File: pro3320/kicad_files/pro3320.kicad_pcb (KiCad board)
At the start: 2 copper layers, 68.3 x 99.1 mm, 82 parts, among them J1 RES_CV, J2 IN, J3 FREQ_CV, J4 EUROPOWER, J5 OUT, J6 OUT2, SW1 LPHP2, SW2 LPHP1, SW3 LPHP3, SW4 LPHP4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

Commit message: pro3320: Fix wrong direction of pots
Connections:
- RV1 pad 1: Net-(R1-Pad2) -> GND
- RV1 pad 3: GND -> Net-(R1-Pad2)
- RV2 pad 1: Net-(J3-Pad2) -> GND
- RV2 pad 3: GND -> Net-(J3-Pad2)
- RV3 pad 1: Net-(J1-Pad2) -> GND
- RV3 pad 3: GND -> Net-(J1-Pad2)
- RV4 pad 1: Net-(C1-Pad2) -> GND
- RV4 pad 3: GND -> Net-(C1-Pad2)
- RV5 pad 1: Net-(R8-Pad1) -> GND
- RV5 pad 3: GND -> Net-(R8-Pad1)
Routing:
- net Net-(R1-Pad2): track 12.5 -> 20.0 mm
- net Net-(J1-Pad2): track 130.5 -> 135.0 mm
- net Net-(J3-Pad2): track 96.7 -> 100.7 mm
- net Net-(R8-Pad1): track 5.17 -> 8.17 mm
- net Net-(C1-Pad2): track 5.04 -> 7.38 mm
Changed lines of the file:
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@@
     (thickness 1.6)
     (drawings 10)
-    (tracks 479)
+    (tracks 484)
     (zones 0)
     (modules 82)
@@
     )
     (pad 3 thru_hole circle (at 0 5) (size 1.8 1.8) (drill 1) (layers *.Cu *.Mask)
-      (net 8 GND))
+      (net 16 "Net-(R1-Pad2)"))
     (pad 2 thru_hole circle (at 0 2.5) (size 1.8 1.8) (drill 1) (layers *.Cu *.Mask)
       (net 19 "Net-(R4-Pad1)"))
     (pad 1 thru_hole circle (at 0 0) (size 1.8 1.8) (drill 1) (layers *.Cu *.Mask)
-      (net 16 "Net-(R1-Pad2)"))
+      (net 8 GND))
     (model ${KISYS3DMOD}/Potentiometer_THT.3dshapes/Potentiometer_Alps_RK097_Single_Horizontal.wrl
       (at (xyz 0 0 0))
@@
     (fp_line (start -2.05 7.25) (end -2.05 -2.25) (layer B.Fab) (width 0.1))
     (pad 1 thru_hole circle (at 0 0) (size 1.8 1.8) (drill 1) (layers *.Cu *.Mask)
-      (net 56 "Net-(J3-Pad2)"))
+      (net 8 GND))
     (pad 2 thru_hole circle (at 0 2.5) (size 1.8 1.8) (drill 1) (layers *.Cu *.Mask)
       (net 20 "Net-(R5-Pad1)"))
     (pad 3 thru_hole circle (at 0 5) (size 1.8 1.8) (drill 1) (layers *.Cu *.Mask)
-      (net 8 GND))
+      (net 56 "Net-(J3-Pad2)"))
     (model ${KISYS3DMOD}/Potentiometer_THT.3dshapes/Potentiometer_Alps_RK097_Single_Horizontal.wrl
       (at (xyz 0 0 0))
@@
     (fp_line (start -2.05 7.25) (end -2.05 -2.25) (layer B.Fab) (width 0.1))
     (pad 1 thru_hole circle (at 0 0) (size 1.8 1.8) (drill 1) (layers *.Cu *.Mask)
-      (net 55 "Net-(J1-Pad2)"))
+      (net 8 GND))
     (pad 2 thru_hole circle (at 0 2.5) (size 1.8 1.8) (drill 1) (layers *.Cu *.Mask)
       (net 27 "Net-(R12-Pad1)"))
     (pad 3 thru_hole circle (at 0 5) (size 1.8 1.8) (drill 1) (layers *.Cu *.Mask)
-      (net 8 GND))
+      (net 55 "Net-(J1-Pad2)"))
     (model ${KISYS3DMOD}/Potentiometer_THT.3dshapes/Potentiometer_Alps_RK097_Single_Horizontal.wrl
       (at (xyz 0 0 0))
@@
     )
     (pad 3 thru_hole circle (at 0 5) (size 1.8 1.8) (drill 1) (layers *.Cu *.Mask)
-      (net 8 GND))
+      (net 1 "Net-(C1-Pad2)"))
     (pad 2 thru_hole circle (at 0 2.5) (size 1.8 1.8) (drill 1) (layers *.Cu *.Mask)
       (net 49 "Net-(RV4-Pad2)"))
     (pad 1 thru_hole circle (at 0 0) (size 1.8 1.8) (drill 1) (layers *.Cu *.Mask)
-      (net 1 "Net-(C1-Pad2)"))
+      (net 8 GND))
     (model ${KISYS3DMOD}/Potentiometer_THT.3dshapes/Potentiometer_Alps_RK097_Single_Horizontal.wrl
       (at (xyz 0 0 0))
@@
     )
     (pad 3 thru_hole circle (at 0 5) (size 1.8 1.8) (drill 1) (layers *.Cu *.Mask)
-      (net 8 GND))
+      (net 22 "Net-(R8-Pad1)"))
     (pad 2 thru_hole circle (at 0 2.5) (size 1.8 1.8) (drill 1) (layers *.Cu *.Mask)
       (net 26 "Net-(R11-Pad1)"))
     (pad 1 thru_hole circle (at 0 0) (size 1.8 1.8) (drill 1) (layers *.Cu *.Mask)
-      (net 22 "Net-(R8-Pad1)"))
+      (net 8 GND))
     (model ${KISYS3DMOD}/Potentiometer_THT.3dshapes/Potentiometer_Alps_RK097_Single_Horizontal.wrl
       (at (xyz 0 0 0))
@@
   (gr_line (start 155.956 40.64) (end 155.956 139.7) (layer Edge.Cuts) (width 0.15))
   (segment (start 146.465 43.053) (end 146.018 43.5) (width 0.25) (layer F.Cu) (net 1))
-  (segment (start 150.876 43.053) (end 146.465 43.053) (width 0.25) (layer F.Cu) (net 1))
+  (segment (start 150.571 48.053) (end 150.876 48.053) (width 0.25) (layer B.Cu) (net 1))
+  (segment (start 146.018 43.5) (end 150.571 48.053) (width 0.25) (layer B.Cu) (net 1))
   (segment (start 140.02 43.5) (end 139.7 43.18) (width 0.25) (layer F.Cu) (net 2))
   (segment (start 144.018 43.5) (end 140.02 43.5) (width 0.25) (layer F.Cu) (net 2))
@@
   (segment (start 138.906 119.888) (end 137.382 118.364) (width 0.25) (layer F.Cu) (net 15))
   (segment (start 138.906 125.222) (end 138.906 119.888) (width 0.25) (layer F.Cu) (net 15))
-  (segment (start 145.325999 56.171999) (end 144.526 55.372) (width 0.25) (layer F.Cu) (net 16))
-  (segment (start 149.849001 60.695001) (end 145.325999 56.171999) (width 0.25) (layer F.Cu) (net 16))
-  (segment (start 149.849001 64.378001) (end 149.849001 60.695001) (width 0.25) (layer F.Cu) (net 16))
-  (segment (start 150.749 65.278) (end 149.849001 64.378001) (width 0.25) (layer F.Cu) (net 16))
+  (segment (start 145.325999 56.171999) (end 144.526 55.372) (width 0.25) (layer B.Cu) (net 16))
+  (segment (start 153.797 64.643) (end 145.325999 56.171999) (width 0.25) (layer B.Cu) (net 16))
+  (segment (start 153.797 67.23) (end 153.797 64.643) (width 0.25) (layer B.Cu) (net 16))
+  (segment (start 150.749 70.278) (end 153.797 67.23) (width 0.25) (layer B.Cu) (net 16))
   (segment (start 141.478 64.516) (end 144.526 61.468) (width 0.25) (layer F.Cu) (net 17))
   (segment (start 136.906 64.516) (end 141.478 64.516) (width 0.25) (layer F.Cu) (net 17))
@@
   (segment (start 150.876 97.79) (end 154.12001 94.54599) (width 0.25) (layer F.Cu) (net 18))
   (segment (start 154.12001 94.54599) (end 154.12001 75.49599) (width 0.25) (layer F.Cu) (net 18))
-  (segment (start 149.849001 66.878001) (end 149.682001 66.878001) (width 0.25) (layer F.Cu) (net 19))
-  (segment (start 150.749 67.778) (end 149.849001 66.878001) (width 0.25) (layer F.Cu) (net 19))
-  (segment (start 149.682001 66.878001) (end 148.336 65.532) (width 0.25) (layer F.Cu) (net 19))
-  (segment (start 148.336 62.23) (end 144.526 58.42) (width 0.25) (layer F.Cu) (net 19))
-  (segment (start 148.336 65.532) (end 148.336 62.23) (width 0.25) (layer F.Cu) (net 19))
+  (segment (start 149.849001 66.878001) (end 149.682001 66.878001) (width 0.25) (layer B.Cu) (net 19))
+  (segment (start 150.749 67.778) (end 149.849001 66.878001) (width 0.25) (layer B.Cu) (net 19))
+  (segment (start 149.682001 66.878001) (end 148.336 65.532) (width 0.25) (layer B.Cu) (net 19))
+  (segment (start 148.336 62.23) (end 144.526 58.42) (width 0.25) (layer B.Cu) (net 19))
+  (segment (start 148.336 65.532) (end 148.336 62.23) (width 0.25) (layer B.Cu) (net 19))
   (segment (start 149.849001 111.328001) (end 149.849001 111.241001) (width 0.25) (layer F.Cu) (net 20))
   (segment (start 150.749 112.228) (end 149.849001 111.328001) (width 0.25) (layer F.Cu) (net 20))
@@
   (segment (start 123.19 50.8) (end 127.762 50.8) (width 0.25) (layer B.Cu) (net 21))
   (segment (start 147.193 87.503) (end 146.05 86.36) (width 0.25) (layer F.Cu) (net 22))
-  (segment (start 150.749 87.503) (end 147.193 87.503) (width 0.25) (layer F.Cu) (net 22))
+  (segment (start 147.193 89.027) (end 147.193 87.503) (width 0.25) (layer F.Cu) (net 22))
+  (segment (start 150.749 92.583) (end 147.193 89.027) (width 0.25) (layer F.Cu) (net 22))
   (segment (start 130.81 54.61) (end 131.826 55.626) (width 0.25) (layer F.Cu) (net 23))
   (segment (start 130.81 50.8) (end 130.81 54.61) (width 0.25) (layer F.Cu) (net 23))
@@
   (segment (start 102.362 106.172) (end 100.33 108.204) (width 0.25) (layer B.Cu) (net 54))
   (segment (start 112.288 114.3) (end 104.16 106.172) (width 0.25) (layer B.Cu) (net 54))
-  (segment (start 155.448 41.91) (end 154.57801 41.04001) (width 0.25) (layer F.Cu) (net 55))
-  (segment (start 155.448 129.54) (end 155.448 41.91) (width 0.25) (layer F.Cu) (net 55))
-  (segment (start 154.57801 41.04001) (end 121.51999 41.04001) (width 0.25) (layer F.Cu) (net 55))
   (segment (start 121.51999 41.04001) (end 119.38 43.18) (width 0.25) (layer F.Cu) (net 55))
-  (segment (start 153.035 131.953) (end 155.448 129.54) (width 0.25) (layer F.Cu) (net 55))
-  (segment (start 150.876 131.953) (end 153.035 131.953) (width 0.25) (layer F.Cu) (net 55))
-  (segment (start 152.4 109.728) (end 150.749 109.728) (width 0.25) (layer F.Cu) (net 56))
-  (segment (start 154.94 107.188) (end 152.4 109.728) (width 0.25) (layer F.Cu) (net 56))
-  (segment (start 154.99799 42.22199) (end 154.99799 53.28201) (width 0.25) (layer F.Cu) (net 56))
-  (segment (start 154.26602 41.49002) (end 154.99799 42.22199) (width 0.25) (layer F.Cu) (net 56))
-  (segment (start 154.99799 53.28201) (end 154.94 53.34) (width 0.25) (layer F.Cu) (net 56))
-  (segment (start 131.22998 41.49002) (end 154.26602 41.49002) (width 0.25) (layer F.Cu) (net 56))
-  (segment (start 154.94 53.34) (end 154.94 107.188) (width 0.25) (layer F.Cu) (net 56))
-  (segment (start 129.54 43.18) (end 131.22998 41.49002) (width 0.25) (layer F.Cu) (net 56))
+  (segment (start 154.57801 41.04001) (end 121.51999 41.04001) (width 0.25) (layer F.Cu) (net 55))
+  (segment (start 152.654 136.447792) (end 152.654 132.334) (width 0.25) (layer F.Cu) (net 55))
+  (segment (start 155.448 129.54) (end 155.448 41.91) (width 0.25) (layer F.Cu) (net 55))
+  (segment (start 152.148792 136.953) (end 152.654 136.447792) (width 0.25) (layer F.Cu) (net 55))
+  (segment (start 155.448 41.91) (end 154.57801 41.04001) (width 0.25) (layer F.Cu) (net 55))
+  (segment (start 152.654 132.334) (end 155.448 129.54) (width 0.25) (layer F.Cu) (net 55))
+  (segment (start 150.876 136.953) (end 152.148792 136.953) (width 0.25) (layer F.Cu) (net 55))
+  (segment (start 131.22998 41.49002) (end 129.54 43.18) (width 0.25) (layer F.Cu) (net 56))
+  (segment (start 154.99799 42.22199) (end 154.26602 41.49002) (width 0.25) (layer F.Cu) (net 56))
+  (segment (start 154.99799 53.28201) (end 154.99799 42.22199) (width 0.25) (layer F.Cu) (net 56))
+  (segment (start 154.26602 41.49002) (end 131.22998 41.49002) (width 0.25) (layer F.Cu) (net 56))
+  (segment (start 152.654 112.823) (end 152.654 109.474) (width 0.25) (layer F.Cu) (net 56))
+  (segment (start 154.94 53.34) (end 154.99799 53.28201) (width 0.25) (layer F.Cu) (net 56))
+  (segment (start 154.94 107.188) (end 154.94 53.34) (width 0.25) (layer F.Cu) (net 56))
+  (segment (start 152.654 109.474) (end 154.94 107.188) (width 0.25) (layer F.Cu) (net 56))
+  (segment (start 150.749 114.728) (end 152.654 112.823) (width 0.25) (layer F.Cu) (net 56))
   (segment (start 138.726 137.16) (end 138.906 137.34) (width 0.25) (layer F.Cu) (net 57))
   (segment (start 129.54 137.16) (end 138.726 137.16) (width 0.25) (layer F.Cu) (net 57))

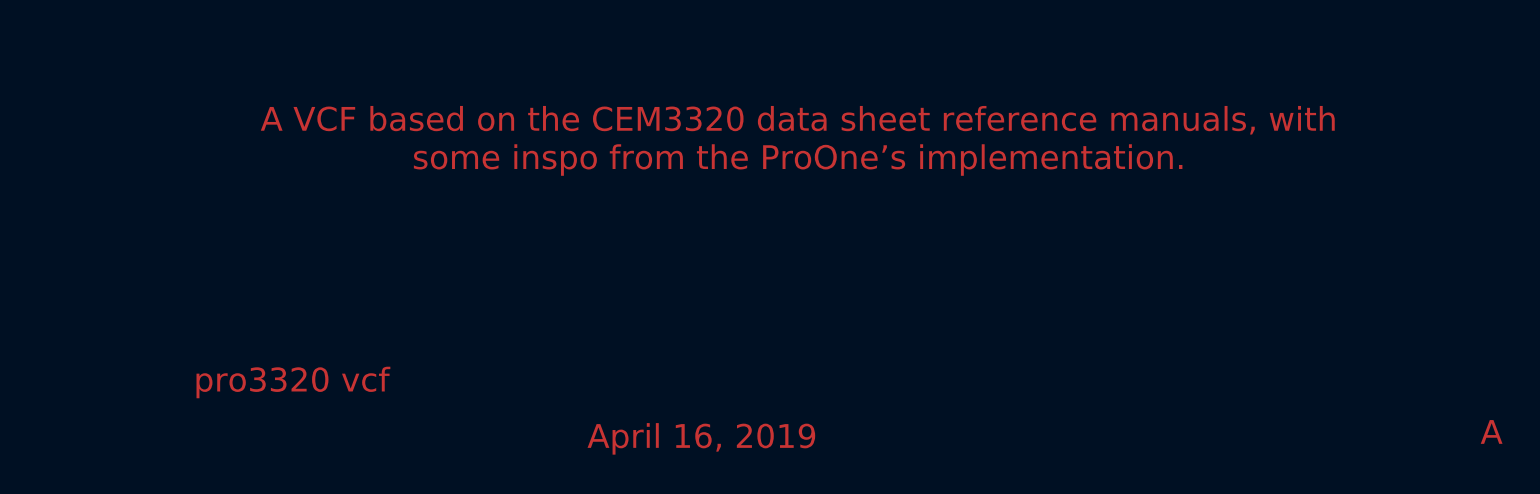
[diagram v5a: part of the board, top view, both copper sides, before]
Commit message: minidrum: Move switches apart a bit
Experiments with PCB layout on paper indicated that the
space between switches was too tight. Maybe still, but better.

Also cleaning up other PCBs a bit.
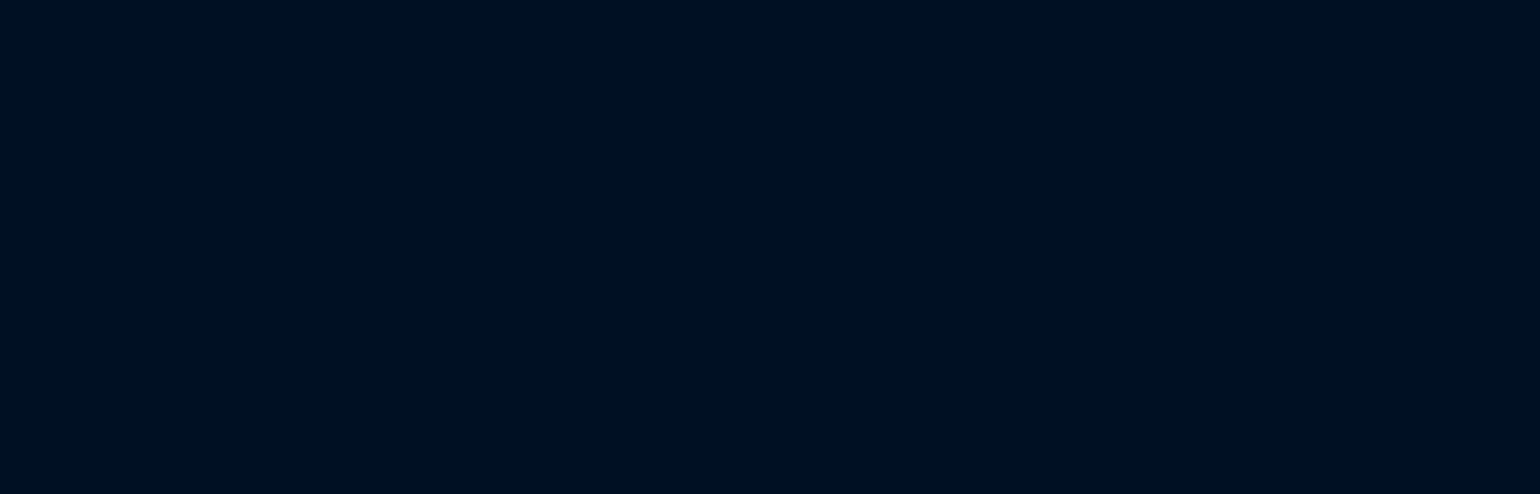
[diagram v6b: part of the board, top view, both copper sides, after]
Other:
- board text added: "A VCF based on the CEM3320 data sheet reference manuals, with some inspo from the ProOne’s implementation. Håkan Eriksson"
- board text removed: "A VCF based on the CEM3320 data sheet reference manuals, with some inspo from the ProOne’s implementation."
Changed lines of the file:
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@@
     (effects (font (size 1.1 1) (thickness 0.2)))
   )
-  (gr_text "April 16, 2019\n" (at 221.488 193.04) (layer F.Cu)
+  (gr_text "April 16, 2019\n" (at 221.488 193.04) (layer Cmts.User)
     (effects (font (size 1.5 1.5) (thickness 0.3)))
   )
-  (gr_text "pro3320 vcf\n" (at 195.58 189.484) (layer F.Cu)
+  (gr_text "pro3320 vcf\n" (at 195.58 189.484) (layer Cmts.User)
     (effects (font (size 1.5 1.5) (thickness 0.3)))
   )
-  (gr_text A (at 271.272 192.786) (layer F.Cu)
+  (gr_text A (at 271.272 192.786) (layer Cmts.User)
     (effects (font (size 1.5 1.5) (thickness 0.3)))
   )
-  (gr_text "A VCF based on the CEM3320 data sheet reference manuals, with\nsome inspo from the ProOne’s implementation." (at 227.584 174.244) (layer F.Cu)
+  (gr_text "A VCF based on the CEM3320 data sheet reference manuals, with\nsome inspo from the ProOne’s implementation.\n\nHåkan Eriksson" (at 227.584 174.244) (layer Cmts.User)
     (effects (font (size 1.5 1.5) (thickness 0.3)))
   )
